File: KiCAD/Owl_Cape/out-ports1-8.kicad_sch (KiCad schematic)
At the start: 42 parts, among them IC1 SN74HC244N, J1 G D V, J2 G D V, J3 G D V, J4 G D V, J5 G D V, J6 G D V, J7 G D V, J8 G D V

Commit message: started routing cu
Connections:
- net V5Rail renamed +5V
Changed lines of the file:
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@@
   (junction (at 156.21 49.53) (diameter 0) (color 0 0 0 0)
   )
+  (junction (at 55.88 123.19) (diameter 0) (color 0 0 0 0)
+  )
   (junction (at 121.92 49.53) (diameter 0) (color 0 0 0 0)
   )
@@
   (junction (at 218.44 49.53) (diameter 0) (color 0 0 0 0)
   )
+  (junction (at 85.09 93.98) (diameter 0) (color 0 0 0 0)
+  )
   (wire (pts (xy 135.89 80.01) (xy 135.89 115.57))
     (stroke (width 0) (type default) (color 0 0 0 0))
@@
     (stroke (width 0) (type default) (color 0 0 0 0))
   )
+  (wire (pts (xy 85.09 78.74) (xy 85.09 87.63))
+    (stroke (width 0) (type default) (color 0 0 0 0))
+  )
   (wire (pts (xy 54.61 113.03) (xy 57.15 113.03))
     (stroke (width 0) (type default) (color 0 0 0 0))
@@
     (stroke (width 0) (type default) (color 0 0 0 0))
   )
+  (wire (pts (xy 85.09 93.98) (xy 85.09 100.33))
+    (stroke (width 0) (type default) (color 0 0 0 0))
+  )
   (wire (pts (xy 85.09 120.65) (xy 153.67 120.65))
     (stroke (width 0) (type default) (color 0 0 0 0))
@@
     (stroke (width 0) (type default) (color 0 0 0 0))
   )
-  (wire (pts (xy 85.09 87.63) (xy 85.09 100.33))
-    (stroke (width 0) (type default) (color 0 0 0 0))
-  )
   (wire (pts (xy 85.09 113.03) (xy 86.36 113.03))
     (stroke (width 0) (type default) (color 0 0 0 0))
@@
     (stroke (width 0) (type default) (color 0 0 0 0))
   )
+  (wire (pts (xy 85.09 87.63) (xy 85.09 93.98))
+    (stroke (width 0) (type default) (color 0 0 0 0))
+  )
   (wire (pts (xy 215.9 80.01) (xy 215.9 137.16))
     (stroke (width 0) (type default) (color 0 0 0 0))
   )
+  (wire (pts (xy 55.88 123.19) (xy 57.15 123.19))
+    (stroke (width 0) (type default) (color 0 0 0 0))
+  )
   (wire (pts (xy 198.12 49.53) (xy 204.47 49.53))
     (stroke (width 0) (type default) (color 0 0 0 0))
@@
     (stroke (width 0) (type default) (color 0 0 0 0))
   )
-  (wire (pts (xy 53.34 123.19) (xy 57.15 123.19))
+  (wire (pts (xy 53.34 123.19) (xy 55.88 123.19))
     (stroke (width 0) (type default) (color 0 0 0 0))
   )
@@
   )
   (wire (pts (xy 54.61 107.95) (xy 57.15 107.95))
-    (stroke (width 0) (type default) (color 0 0 0 0))
-  )
-  (wire (pts (xy 85.09 78.74) (xy 85.09 87.63))
     (stroke (width 0) (type default) (color 0 0 0 0))
   )
@@
     (property "Intersheet References" "${INTERSHEET_REFS}" (id 0) (at 0 0 0)
       (effects (font (size 1.27 1.27)) hide)
-    )
-  )
-  (global_label "V5Rail" (shape input) (at 85.09 78.74 90) (fields_autoplaced)
-    (effects (font (size 1.27 1.27)) (justify left))
-    (property "Intersheet References" "${INTERSHEET_REFS}" (id 0) (at 85.0106 70.4287 90)
-      (effects (font (size 1.27 1.27)) (justify left) hide)
     )
   )
@@
     (pin "2")
   )
+  (symbol (lib_id "power:PWR_FLAG") (at 55.88 123.19 0) (unit 1)
+    (in_bom yes) (on_board yes) (fields_autoplaced)
+    (property "Reference" "#FLG0103" (id 0) (at 55.88 121.285 0)
+      (effects (font (size 1.27 1.27)) hide)
+    )
+    (property "Value" "PWR_FLAG" (id 1) (at 55.88 119.6142 0))
+    (property "Footprint" "" (id 2) (at 55.88 123.19 0)
+      (effects (font (size 1.27 1.27)) hide)
+    )
+    (property "Datasheet" "~" (id 3) (at 55.88 123.19 0)
+      (effects (font (size 1.27 1.27)) hide)
+    )
+    (pin "1")
+  )
+  (symbol (lib_id "power:+5V") (at 85.09 78.74 0) (unit 1)
+    (in_bom yes) (on_board yes) (fields_autoplaced)
+    (property "Reference" "#PWR0124" (id 0) (at 85.09 82.55 0)
+      (effects (font (size 1.27 1.27)) hide)
+    )
+    (property "Value" "+5V" (id 1) (at 85.09 75.1642 0))
+    (property "Footprint" "" (id 2) (at 85.09 78.74 0)
+      (effects (font (size 1.27 1.27)) hide)
+    )
+    (property "Datasheet" "" (id 3) (at 85.09 78.74 0)
+      (effects (font (size 1.27 1.27)) hide)
+    )
+    (pin "1")
+  )
+  (symbol (lib_id "power:PWR_FLAG") (at 85.09 93.98 0) (unit 1)
+    (in_bom yes) (on_board yes) (fields_autoplaced)
+    (property "Reference" "#FLG0104" (id 0) (at 85.09 92.075 0)
+      (effects (font (size 1.27 1.27)) hide)
+    )
+    (property "Value" "PWR_FLAG" (id 1) (at 85.09 90.4042 0))
+    (property "Footprint" "" (id 2) (at 85.09 93.98 0)
+      (effects (font (size 1.27 1.27)) hide)
+    )
+    (property "Datasheet" "~" (id 3) (at 85.09 93.98 0)
+      (effects (font (size 1.27 1.27)) hide)
+    )
+    (pin "1")
+  )
 )

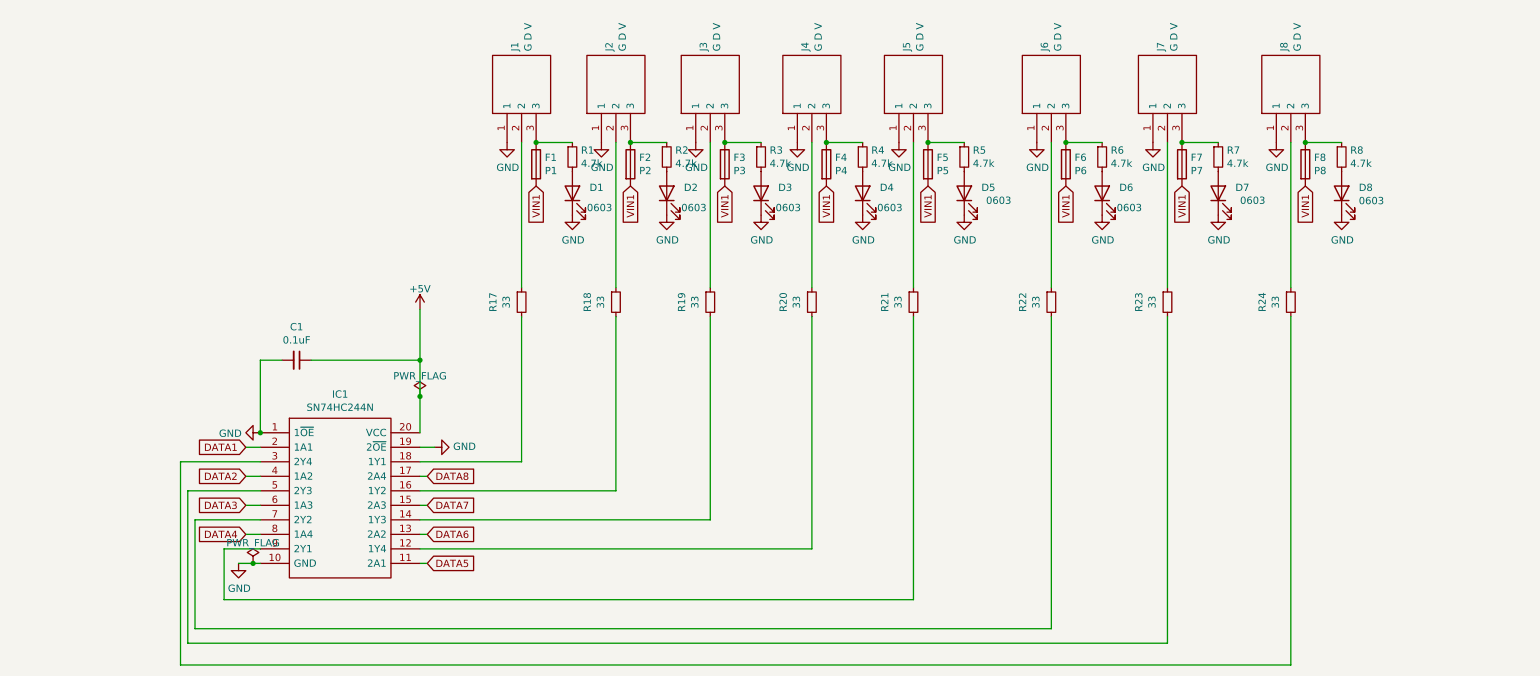
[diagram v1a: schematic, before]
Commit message: swap chips to better speed / layout
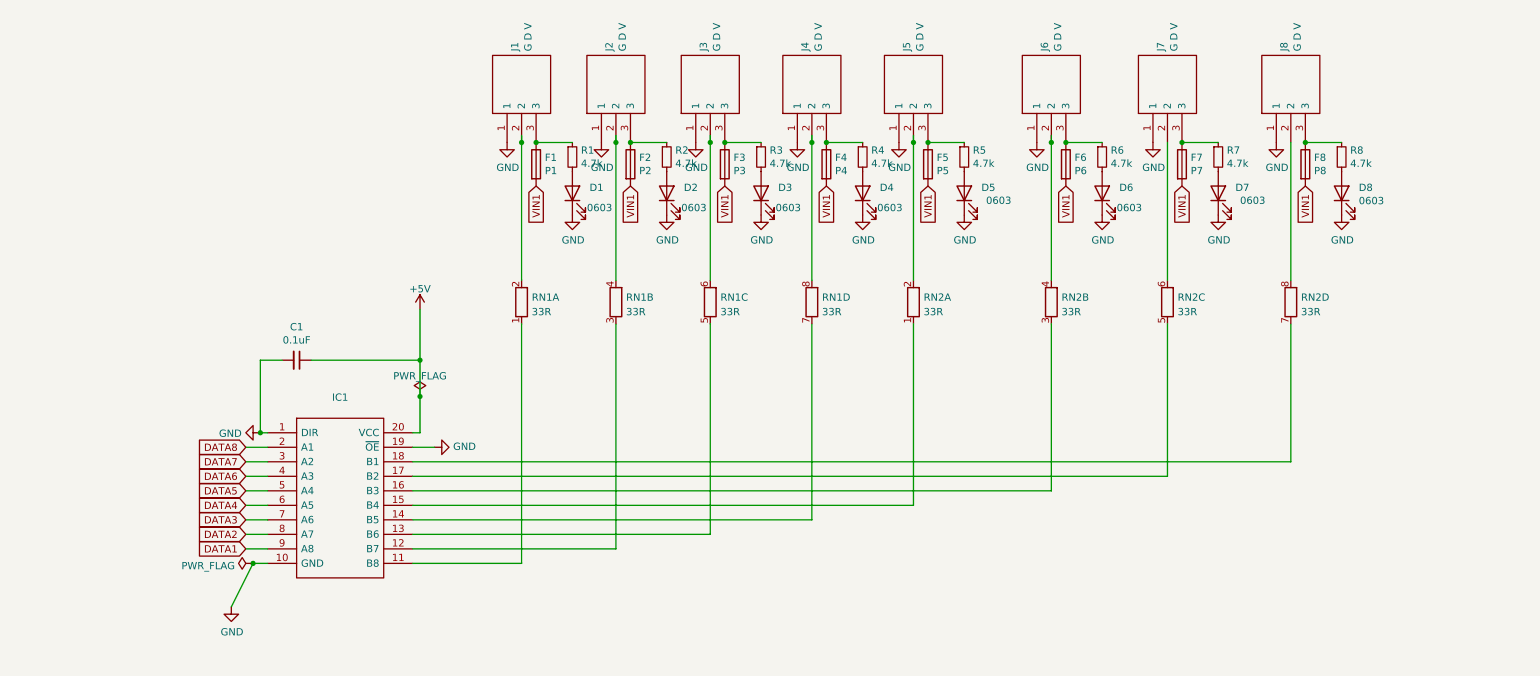
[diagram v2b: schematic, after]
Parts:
- removed IC1: SN74HC244N, SamacSys_Parts:DIP794W53P254L2540H508Q20N, symbol owl_cape-rescue:SN74HC244N-SamacSys_Parts
- removed R17, R18, R19, R20, R21, R22, R23, R24: 33, Resistor_SMD:R_0805_2012Metric, symbol Device:R_Small
- added IC1: (no value), symbol SamacSys_Parts:SN74AHC245N
- added RN1, RN2: 33R, Resistor_THT:R_Array_SIP8, symbol Device:R_Pack04_SIP_Split
- F1: footprint Fuse:Fuseholder_Blade_Mini_Keystone_3568 -> Stuart_BESPOKE:Medium Auto Fuse Holder
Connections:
- net +5V: now also IC1.20 (VCC)
- net DATA1: now also IC1.9 (A8)
- net DATA2: now also IC1.8 (A7)
- net DATA3: now also IC1.7 (A6)
- net DATA4: now also IC1.6 (A5)
- net DATA5: now also IC1.5 (A4)
- net DATA6: now also IC1.4 (A3)
- net DATA7: now also IC1.3 (A2)
- net DATA8: now also IC1.2 (A1)
- net GND: now also IC1.1 (DIR), IC1.10 (GND), IC1.19 (~{OE})
- net at J2.2: now also RN1.4 (R2.2)
- net at J3.2: now also RN1.6 (R3.2)
- net at J4.2: now also RN1.8 (R4.2)
- net at J5.2: now also RN2.2 (R1.2)
- net at J6.2: now also RN2.4 (R2.2)
- net at J7.2: now also RN2.6 (R3.2)
- net at J8.2: now also RN2.8 (R4.2)
- net at J1.2: now also RN1.2 (R1.2)
- new net: IC1.13 (B6), RN1.5 (R3.1)
- new net: IC1.12 (B7), RN1.3 (R2.1)
- new net: IC1.17 (B2), RN2.5 (R3.1)
- new net: IC1.16 (B3), RN2.3 (R2.1)
- new net: IC1.11 (B8), RN1.1 (R1.1)
- new net: IC1.14 (B5), RN1.7 (R4.1)
- new net: IC1.15 (B4), RN2.1 (R1.1)
- new net: IC1.18 (B1), RN2.7 (R4.1)

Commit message: major update to layout
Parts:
- removed F7: P7, Fuse:Fuseholder_Blade_Mini_Keystone_3568, symbol Device:Fuse
- added F7: P7, Stuart_BESPOKE:Medium Auto Fuse Holder, symbol Stuarts_BESPOKE:Medium_Auto_Fuse_Holder
- F1: symbol Device:Fuse -> Stuarts_BESPOKE:Medium_Auto_Fuse_Holder
- F2, F3, F4, F5, F6, F8: footprint Fuse:Fuseholder_Blade_Mini_Keystone_3568 -> Stuart_BESPOKE:Medium Auto Fuse Holder; symbol Device:Fuse -> Stuarts_BESPOKE:Medium_Auto_Fuse_Holder
- IC1: value (none) -> SN74AHC245N; footprint (none) -> DIP794W53P254L2540H508Q20N
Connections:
- net +5V: now also IC1.1 (DIR)
- net GND: no longer IC1.1 (DIR)
- net VIN1: now also F1.1, F2.1, F3.1, F4.1, F5.1, F6.1, F8.1, F7.1, F7.2
- net at J2.3, R2.1: now also F2.3, F2.4; no longer F2.1
- net at J3.3, R3.1: now also F3.3, F3.4; no longer F3.1
- net at J4.3, R4.1: now also F4.3, F4.4; no longer F4.1
- net at J5.3, R5.1: now also F5.3, F5.4; no longer F5.1
- net at J6.3, R6.1: now also F6.3, F6.4; no longer F6.1
- net at J7.3, R7.1: now also F7.3, F7.4
- net at J8.3, R8.1: now also F8.3, F8.4; no longer F8.1
- net at J1.3, R1.1: now also F1.3, F1.4; no longer F1.1
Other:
- moved on the sheet: C1, D1, D2, D4, D5, D6, D7, D8, IC1, J1, J2, J4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
